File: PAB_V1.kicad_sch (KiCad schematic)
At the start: 64 parts, among them J1 Screw_Terminal_01x02, J10 Conn_01x01_Socket, J11 Conn_01x01_Socket, J12 Conn_01x01_Socket, J13 Conn_01x01_Socket, J14 Conn_01x01_Socket, J15 Conn_01x01_Socket, J16 Conn_01x01_Socket, J17 Conn_01x01_Socket, J18 Conn_01x01_Socket, J19 Conn_01x01_Socket, J2 USB_C_Receptacle_USB2.0_14P, J20 Conn_01x01_Socket, J21 Conn_01x01_Socket, J22 Conn_01x01_Socket, J23 Conn_01x01_Socket, J24 Conn_01x01_Socket, J25 Conn_01x01_Socket, J26 Conn_01x01_Socket, J3 Screw_Terminal_01x06, J4 Conn_01x01_Socket, J5 Conn_01x01_Socket, J6 Conn_01x01_Socket, J7 Conn_01x01_Socket, J8 Conn_01x01_Socket, J9 Conn_01x01_Socket, Q1 Red, Q2 Green, Q3 Blue, Q4 White, Q5 White, SW1 RESET, SW2 BOOT, U1 AP63205WU-7, U2 TPS2116DRLR, U3 INTERFACE-CP2102-GMR_QFN28_, U4 AP63203WU, U5 ESP32-S3-MINI-1, U6 TPD4E05U06DQAR

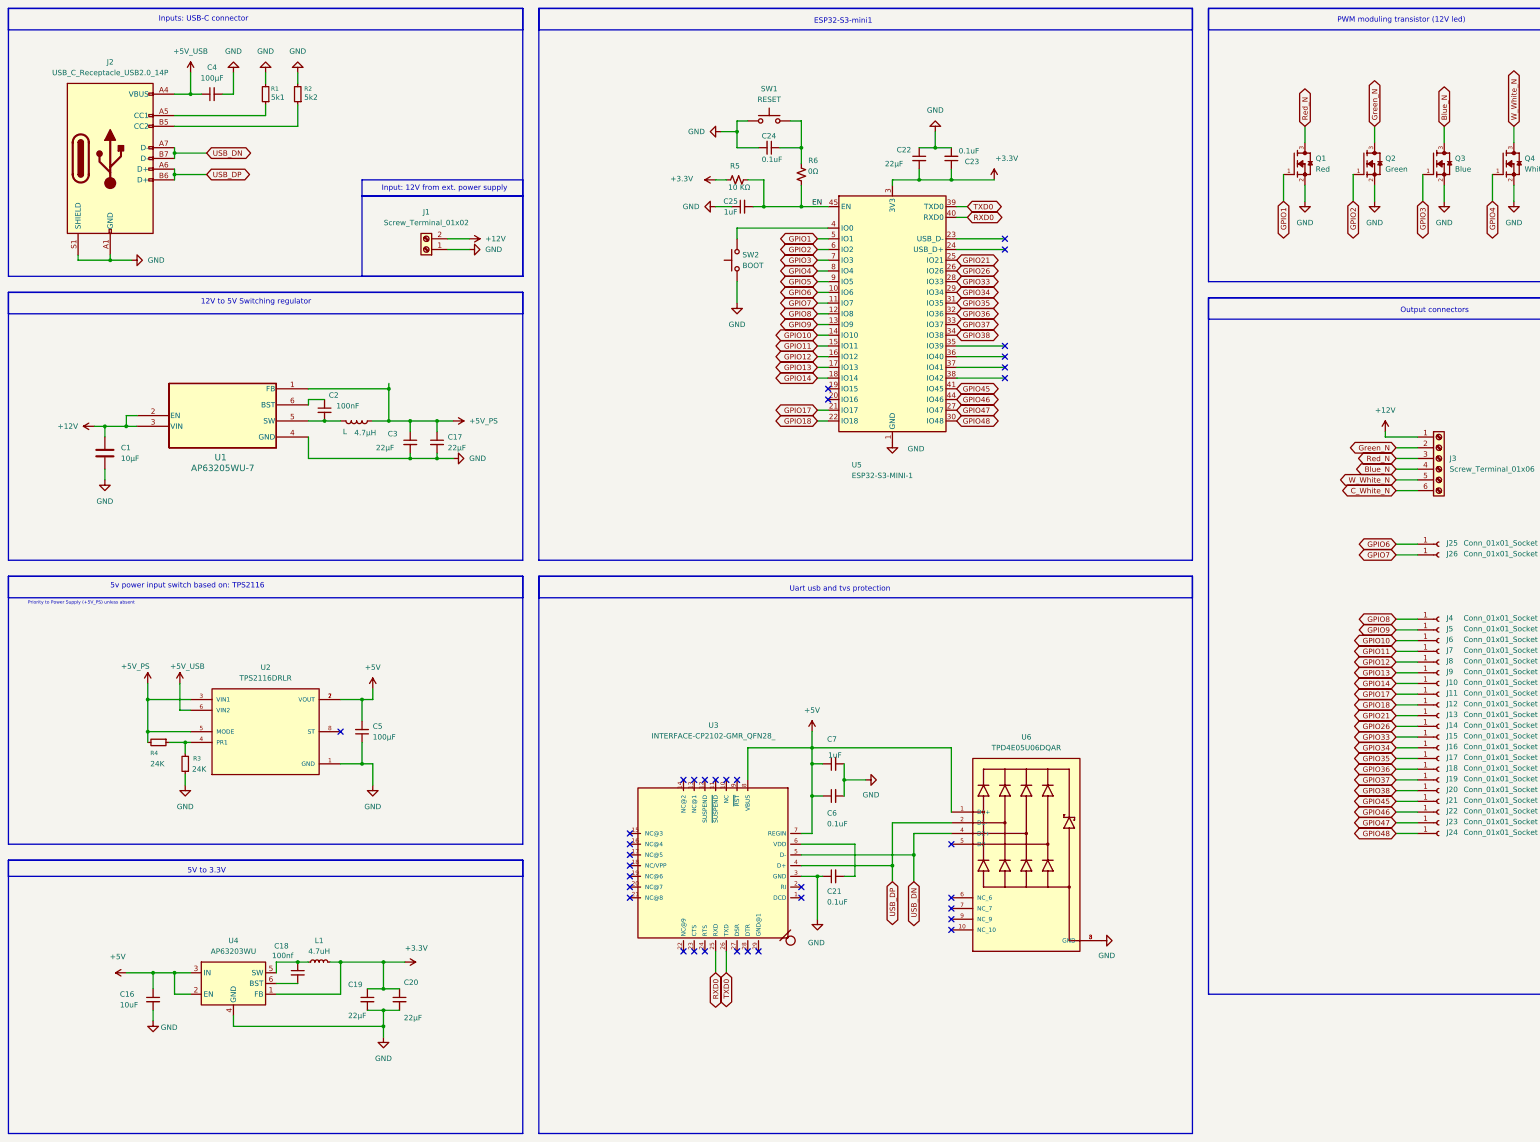
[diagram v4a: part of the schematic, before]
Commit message: Added TVS to 12V input, reorganized names, reorganized structures
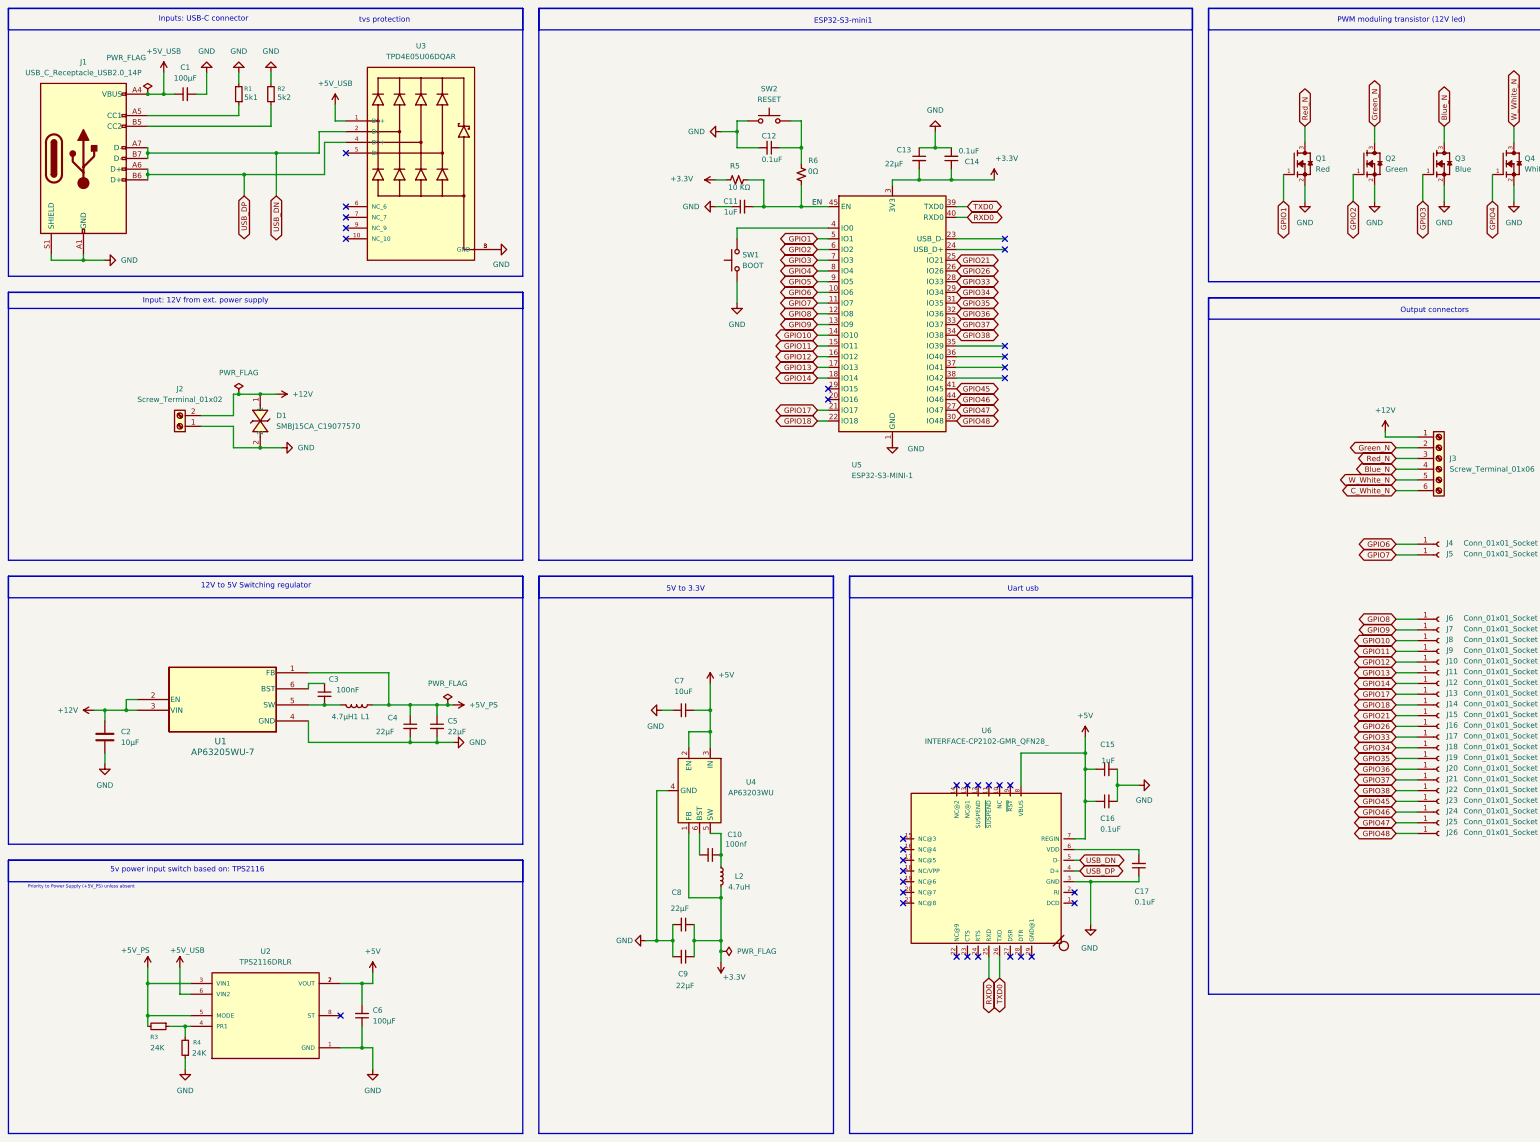
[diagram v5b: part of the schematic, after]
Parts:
- added D1: SMBJ15CA_C19077570, easyeda2kicad:SMB_L4.6-W3.6-LS5.4-BI, symbol easyeda2kicad:SMBJ15CA_C19077570
- L1: renamed from 4.7μH; value L -> 4.7μH1
- U1: footprint SOIC_05WU-7_DIO -> Footprint:SOIC_05WU-7_DIO
- renumbered C4 to C1, C18 to C10, C25 to C11, C24 to C12, C22 to C13, C23 to C14, C7 to C15, C6 to C16, C21 to C17, C1 to C2, C2 to C3, C3 to C4, C17 to C5, C5 to C6, C16 to C7, C19 to C8, C20 to C9, J2 to J1, J8 to J10, J9 to J11, J10 to J12, J11 to J13, J12 to J14, J13 to J15, J14 to J16, J15 to J17, J16 to J18, J17 to J19, J1 to J2, J18 to J20, J19 to J21, J20 to J22, J21 to J23, J22 to J24, J23 to J25, J24 to J26, J25 to J4, J26 to J5, J4 to J6, J5 to J7, J6 to J8, J7 to J9, L1 to L2, R4 to R3, R3 to R4, SW2 to SW1, SW1 to SW2, U6 to U3, U3 to U6
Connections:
- net +12V: now also D1.1
- net +5V: no longer U3.1 (D1+)
- net +5V_USB: now also U3.1 (D1+)
- net GND: now also D1.2
- net USB_DN: now also U3.2 (D1-); no longer U3.4 (D2+)
- net USB_DP: now also U3.4 (D2+); no longer U3.2 (D1-)
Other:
- note added: "Uart usb"
- note added: "tvs protection"
- note removed: "Uart usb and tvs protection"
- moved on the sheet: C1, C10, C15, C16, C17, C2, C3, C4, C5, C6, C7, C8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

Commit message: Changed whole symbol and footprint library, used easyeda2kicad converted from jlc part.
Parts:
- removed C1: 100μF, symbol Device:C_Small
- removed C10: 100nf, symbol Device:C_Small
- removed C11: 1uF, symbol Device:C_Small
- removed C12, C14: 0.1uF, symbol Device:C_Small
- removed C13, C8, C9: 22μF, symbol Device:C_Small
- removed D1: SMBJ15CA_C19077570, easyeda2kicad:SMB_L4.6-W3.6-LS5.4-BI, symbol easyeda2kicad:SMBJ15CA_C19077570
- removed J1: USB_C_Receptacle_USB2.0_14P, symbol Connector:USB_C_Receptacle_USB2.0_14P
- removed J10, J11, J12, J13, J14, J15, J16, J17, J18, J19, J20, J21, J22, J23, J24, J25, J26, J4, J5, J6, J7, J8, J9: Conn_01x01_Socket, symbol Connector:Conn_01x01_Socket
- removed L2: 4.7uH, symbol Device:L_Small
- removed Q1: Red, AO3400A:SOT95P280X125-3N, symbol AO3400A:AO3400A
- removed Q2: Green, AO3400A:SOT95P280X125-3N, symbol AO3400A:AO3400A
- removed Q3: Blue, AO3400A:SOT95P280X125-3N, symbol AO3400A:AO3400A
- removed Q4, Q5: White, AO3400A:SOT95P280X125-3N, symbol AO3400A:AO3400A
- removed R1: 5k1, symbol Device:R_Small
- removed R2: 5k2, symbol Device:R_Small
- removed R5: 10 KΩ, symbol Device:R_Small_US
- removed R6: 0Ω, symbol Device:R_Small_US
- removed SW1: BOOT, symbol Switch:SW_Push
- removed SW2: RESET, symbol Switch:SW_Push
- removed U1: AP63205WU-7, Footprint:SOIC_05WU-7_DIO, symbol 2025-07-07_14-46-04:AP63205WU-7
- removed U2: TPS2116DRLR, TPS2116DRLR:SOTFL50P160X60-8N, symbol TPS2116DRLR:TPS2116DRLR
- removed U3: TPD4E05U06DQAR, TPD4E05U06DQAR:IC_TPD4E05U06DQAR, symbol TPD4E05U06DQAR:TPD4E05U06DQAR
- removed U4: AP63203WU, Package_TO_SOT_SMD:TSOT-23-6, symbol Regulator_Switching:AP63203WU
- removed U5: ESP32-S3-MINI-1, RF_Module:ESP32-S2-MINI-1, symbol RF_Module:ESP32-S3-MINI-1
- removed U6: INTERFACE-CP2102-GMR_QFN28_, INTERFACE-CP2102-GMR_QFN28_:QFN28G_0.5-5X5MM, symbol INTERFACE-CP2102-GMR_QFN28_:INTERFACE-CP2102-GMR_QFN28_
- added C18: 1uF, symbol Device:C_Small
- added C19, C21: 0.1uF, symbol Device:C_Small
- added C20, C23, C24: 22μF, symbol Device:C_Small
- added C22: 10uF, symbol Device:C_Small
- added C25: 100nf, symbol Device:C_Small
- added D1: SMBJ15CA_C78809, Footprint:SMB_L4.6-W3.6-LS5.3-BI, symbol SMBJ15CA_C78809:SMBJ15CA_C78809
- added D3: TPD4E05U06DQAR_C138714, Footprint:USON-10_L2.5-W1.0-P0.50-BL, symbol TPD4E05U06DQAR_C138714:TPD4E05U06DQAR_C138714
- added J10, J11, J12, J13, J14, J15, J16, J17, J18, J19, J20, J21, J22, J23, J24, J25, J26, J4, J5, J6, J7, J8, J9: Conn_01x01, symbol Connector_Generic:Conn_01x01
- added L3: 4.7uH, symbol Device:L_Small
- added Q1, Q2, Q3, Q4, Q5: AO3400A, Package_TO_SOT_SMD:SOT-23, symbol Transistor_FET:AO3400A
- added R10, R9: 24K, symbol Device:R_Small
- added R7: 10 KΩ, symbol Device:R_Small_US
- added R8: 0Ω, symbol Device:R_Small_US
- added SW3: RESET, symbol Switch:SW_Push
- added SW4: BOOT, symbol Switch:SW_Push
- added U1: AP63205WU-7, Footprint:TSOT-23-6_L2.9-W1.6-P0.95-LS2.8-BL, symbol AP63205WU-7:AP63205WU-7
- added U2: AP63203WU-7, Footprint:TSOT-26_L2.9-W1.6-P0.95-LS2.8-BL, symbol AP63203WU-7:AP63203WU-7
- added U3: CP2102-GMR, Footprint:WQFN-28_L5.0-W5.0-P0.50-BL-EP3.2, symbol CP2102-GMR:CP2102-GMR
- added U4: TPS2116DRL, Package_TO_SOT_SMD:SOT-583-8, symbol Power_Management:TPS2116DRL
- added U6: ESP32-S3-MINI-1-N4R2, Footprint:BULETM-SMD_ESP32-S3-MINI-1-N8, symbol ESP32-S3-MINI-1-N4R2:ESP32-S3-MINI-1-N4R2
- added USB2: TYPE-C16PIN, Footprint:USB-C-SMD_TYPE-C16PIN, symbol TYPE-C16PIN:TYPE-C16PIN
- C6: value 100μF -> 10μF
- C7: value 10uF -> 100μF
- R3: value 24K -> 5k1
- R4: value 24K -> 5k2
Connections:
- net +12V: now also D1.2 (A), U1.2 (EN), U1.3 (VIN)
- net +3.3V: now also C20.2, C21.1, C23.1, C24.1, L3.2, R7.2, U2.1 (FB), U6.3 (3V3)
- net +5V: now also C7.2, C22.1, U2.2 (EN), U2.3 (VIN), U3.7 (REGIN), U3.8 (VBUS), U4.2 (VOUT), U4.7 (VOUT); no longer C6.2, C7.1
- net +5V_PS: now also R9.2, U1.1 (FB), U4.3 (VIN1), U4.5 (MODE); no longer R3.2
- net +5V_USB: now also C6.1, D3.4 (D2+), U4.6 (VIN2), USB2.A4B9 (VBUS), USB2.B4A9 (VBUS)
- net Blue_N: now also Q3.3 (D)
- net C_White_N: now also Q5.3 (D)
- net EN: now also C18.2, R7.1, R8.2, U6.45 (EN)
- net GND: now also C6.2, C7.1, R3.2, R4.2, C18.1, C19.2, C20.1, C21.2, C22.2, C23.2, C24.2, D1.1 (K), D3.3 (GND), D3.8 (GND), Q1.2 (S), Q2.2 (S), Q3.2 (S), Q4.2 (S), Q5.2 (S), R10.1, SW3.1, SW4.1, U1.4 (GND), U2.4 (GND), U3.3 (GND), U4.1 (GND), U6.1 (GND), U6.2 (GND), U6.42 (GND), U6.43 (GND), U6.46 (GND), U6.47 (GND), U6.48 (GND), U6.49 (GND), U6.50 (GND), U6.51 (GND), U6.52 (GND), U6.53 (GND), U6.54 (GND), U6.55 (GND), U6.56 (GND), U6.57 (GND), U6.58 (GND), U6.59 (GND), U6.60 (GND), U6.GND, USB2.1 (SHELL), USB2.2 (SHELL), USB2.3 (SHELL), USB2.4 (SHELL), USB2.A1B12 (GND), USB2.B1A12 (GND); no longer C6.1, C7.2, R4.1
- net GPIO1: now also Q1.1 (G), U6.5 (IO1)
- net GPIO10: now also J8.1 (Pin_1), U6.14 (IO10)
- net GPIO11: now also J9.1 (Pin_1), U6.15 (IO11)
- net GPIO12: now also J10.1 (Pin_1), U6.16 (IO12)
- net GPIO13: now also J11.1 (Pin_1), U6.17 (IO13)
- net GPIO14: now also J12.1 (Pin_1), U6.18 (IO14)
- net GPIO17: now also J13.1 (Pin_1), U6.21 (IO17)
- net GPIO18: now also J14.1 (Pin_1), U6.22 (IO18)
- net GPIO2: now also Q2.1 (G), U6.6 (IO2)
- net GPIO21: now also J15.1 (Pin_1), U6.25 (IO21)
- net GPIO26: now also J16.1 (Pin_1), U6.26 (IO26)
- net GPIO3: now also Q3.1 (G), U6.7 (IO3)
- net GPIO33: now also J17.1 (Pin_1), U6.28 (IO33)
- net GPIO34: now also J18.1 (Pin_1), U6.29 (IO34)
- net GPIO35: now also J19.1 (Pin_1), U6.31 (IO35)
- net GPIO36: now also J20.1 (Pin_1), U6.32 (IO36)
- net GPIO37: now also J21.1 (Pin_1), U6.33 (IO37)
- net GPIO38: now also J22.1 (Pin_1), U6.34 (IO38)
- net GPIO4: now also Q4.1 (G), U6.8 (IO4)
- net GPIO45: now also J23.1 (Pin_1), U6.41 (IO45)
- net GPIO46: now also J24.1 (Pin_1), U6.44 (IO46)
- net GPIO47: now also J25.1 (Pin_1), U6.27 (IO47)
- net GPIO48: now also J26.1 (Pin_1), U6.30 (IO48)
- net GPIO5: now also Q5.1 (G), U6.9 (IO5)
- net GPIO6: now also J4.1 (Pin_1), U6.10 (IO6)
- net GPIO7: now also J5.1 (Pin_1), U6.11 (IO7)
- net GPIO8: now also J6.1 (Pin_1), U6.12 (IO8)
- net GPIO9: now also J7.1 (Pin_1), U6.13 (IO9)
- net Green_N: now also Q2.3 (D)
- net RXD0: now also U3.25 (RXD), U6.40 (RXD0)
- net Red_N: now also Q1.3 (D)
- net TXD0: now also U3.26 (TXD), U6.39 (TXD0)
- net USB_DN: now also D3.2 (D1-), U3.5 (D-), USB2.A7 (DN1), USB2.B7 (DN2)
- net USB_DP: now also D3.1 (D1+), U3.4 (D+), USB2.A6 (DP1), USB2.B6 (DP2)
- net W_White_N: now also Q4.3 (D)
- net at C3.1: now also U1.6 (BST)
- net at C3.2, L1.2: now also U1.5 (SW)
- net at R3.1: now also USB2.A5 (CC1); no longer R4.2
- net at C17.2: now also U3.6 (VDD)
- new net: R10.2, R9.1, U4.4 (PR1)
- new net: C25.1, L3.1, U2.5 (SW)
- new net: C25.2, U2.6 (BST)
- new net: C19.1, R8.1, SW3.2
- new net: SW4.2, U6.4 (IO0)
- new net: R4.1, USB2.B5 (CC2)
- no-connect marks 35 -> 37
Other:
- moved on the sheet: C2, C3, C4, C5, L1

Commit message: Added most of the component footprint need specs for capacitor types and dimension
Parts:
- J2: footprint (none) -> Footprint:CONN-TH_WJ126V-5.0-2P
- J3: footprint (none) -> Footprint:CONN-TH_6P-P5.00_WJ126V-5.0-6P
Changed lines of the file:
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@@
 			)
 		)
-		(property "Footprint" ""
+		(property "Footprint" "Footprint:CONN-TH_WJ126V-5.0-2P"
 			(at 55.88 114.3 0)
 			(effects
@@
 			)
 		)
-		(property "Footprint" ""
+		(property "Footprint" "Footprint:CONN-TH_6P-P5.00_WJ126V-5.0-6P"
 			(at 354.33 121.92 0)
 			(effects

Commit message: Macbook project test upload
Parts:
- added R7, R8: 22, symbol Device:R_Small
- C12: renamed from C19; footprint (none) -> Capacitor_SMD:C_0201_0603Metric
- renumbered C6 to C1, C23 to C10, C18 to C11, C20 to C13, C21 to C14, C7 to C6, C22 to C7, C25 to C8, C24 to C9, D3 to D2, J2 to J1, J11 to J10, J12 to J11, J13 to J12, J14 to J13, J15 to J14, J16 to J15, J17 to J16, J18 to J17, J19 to J18, J20 to J19, J3 to J2, J21 to J20, J22 to J21, J23 to J22, J24 to J23, J25 to J24, J26 to J25, J4 to J3, J5 to J4, J6 to J5, J7 to J6, J8 to J7, J9 to J8, J10 to J9, L3 to L2, R3 to R1, R4 to R2, R9 to R3, R10 to R4, R7 to R5, R8 to R6, SW3 to SW1, SW4 to SW2, U4 to U2, U2 to U3, U6 to U4, U3 to U5, USB2 to USB1
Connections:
- net USB_DN: now also R8.1; no longer U5.5 (D-)
- net USB_DP: now also R7.2; no longer U5.4 (D+)
- new net: R7.1, U5.4 (D+)
- new net: R8.2, U5.5 (D-)
